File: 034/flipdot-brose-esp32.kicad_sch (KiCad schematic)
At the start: 63 parts, among them J2 Barrel_Jack_Switch, J3 Screw_Terminal_01x02, J5 OLED, J6 TYPE-C-31-M-12, Q11 UMH3N, SW1 CONF, SW2 STAT, SW3 RST, U1 74HCT245, U2 ESP32-WROOM-32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

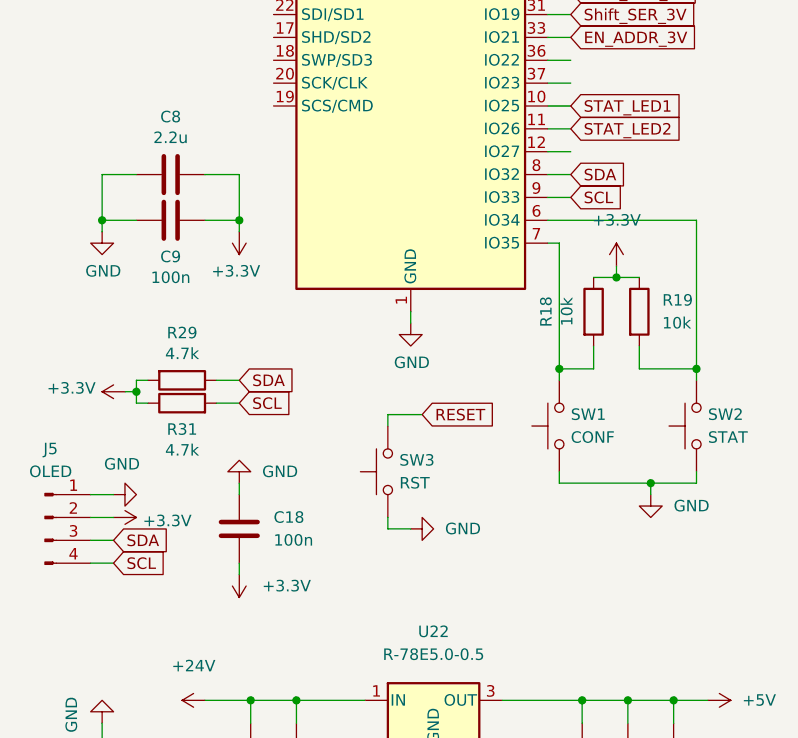
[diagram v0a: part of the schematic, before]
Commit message: fixing naming SDA/SCL
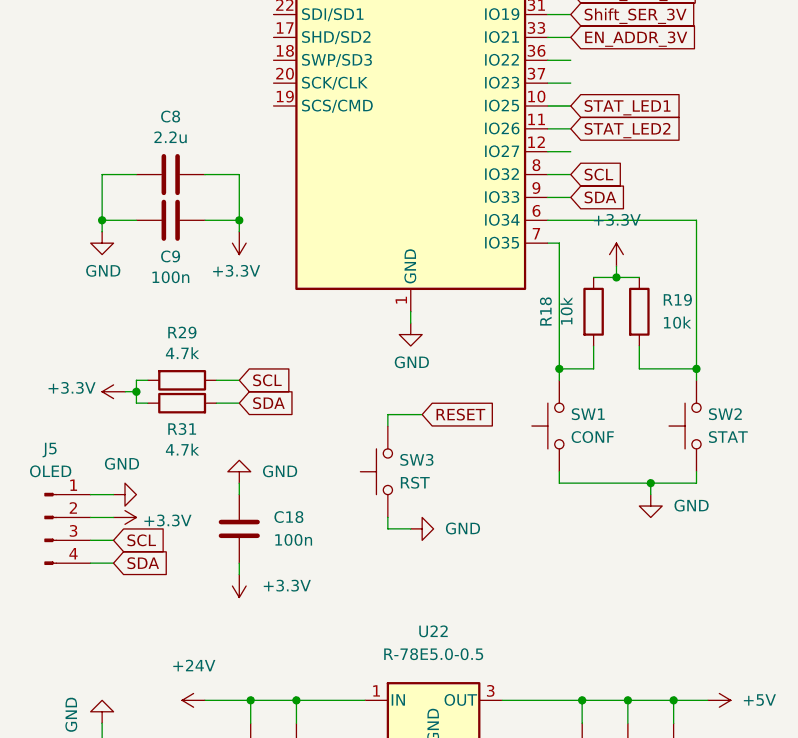
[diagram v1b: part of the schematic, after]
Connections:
- net SCL: now also J5.3 (Pin_3), R29.1, U2.8 (IO32); no longer J5.4 (Pin_4), R31.2, U2.9 (IO33)
- net SDA: now also J5.4 (Pin_4), R31.2, U2.9 (IO33); no longer J5.3 (Pin_3), R29.1, U2.8 (IO32)
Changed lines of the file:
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@@
     (stroke (width 0) (type default) (color 0 0 0 0))
   )
-  (global_label "SDA" (shape input) (at 73.66 80.01 0) (fields_autoplaced)
-    (effects (font (size 1.27 1.27)) (justify left))
-    (property "Intersheet References" "${INTERSHEET_REFS}" (id 0) (at 0 0 0)
-      (effects (font (size 1.27 1.27)) hide)
+  (global_label "SCL" (shape input) (at 73.66 80.01 0) (fields_autoplaced)
+    (effects (font (size 1.27 1.27)) (justify left))
+    (property "Intersheet References" "${INTERSHEET_REFS}" (id 0) (at 79.4918 79.9306 0)
+      (effects (font (size 1.27 1.27)) (justify left) hide)
     )
   )
@@
     )
   )
-  (global_label "SCL" (shape input) (at 36.83 105.41 0) (fields_autoplaced)
-    (effects (font (size 1.27 1.27)) (justify left))
-    (property "Intersheet References" "${INTERSHEET_REFS}" (id 0) (at -12.7 -38.1 0)
-      (effects (font (size 1.27 1.27)) hide)
+  (global_label "SDA" (shape input) (at 36.83 105.41 0) (fields_autoplaced)
+    (effects (font (size 1.27 1.27)) (justify left))
+    (property "Intersheet References" "${INTERSHEET_REFS}" (id 0) (at 42.7223 105.3306 0)
+      (effects (font (size 1.27 1.27)) (justify left) hide)
     )
   )
@@
     )
   )
-  (global_label "SCL" (shape input) (at 22.86 123.19 0) (fields_autoplaced)
-    (effects (font (size 1.27 1.27)) (justify left))
-    (property "Intersheet References" "${INTERSHEET_REFS}" (id 0) (at -26.67 -20.32 0)
-      (effects (font (size 1.27 1.27)) hide)
+  (global_label "SDA" (shape input) (at 22.86 123.19 0) (fields_autoplaced)
+    (effects (font (size 1.27 1.27)) (justify left))
+    (property "Intersheet References" "${INTERSHEET_REFS}" (id 0) (at 28.7523 123.1106 0)
+      (effects (font (size 1.27 1.27)) (justify left) hide)
     )
   )
@@
     )
   )
-  (global_label "SDA" (shape input) (at 22.86 120.65 0) (fields_autoplaced)
-    (effects (font (size 1.27 1.27)) (justify left))
-    (property "Intersheet References" "${INTERSHEET_REFS}" (id 0) (at -26.67 -20.32 0)
-      (effects (font (size 1.27 1.27)) hide)
-    )
-  )
-  (global_label "SDA" (shape input) (at 36.83 102.87 0) (fields_autoplaced)
-    (effects (font (size 1.27 1.27)) (justify left))
-    (property "Intersheet References" "${INTERSHEET_REFS}" (id 0) (at -12.7 -38.1 0)
-      (effects (font (size 1.27 1.27)) hide)
-    )
-  )
-  (global_label "SCL" (shape input) (at 73.66 82.55 0) (fields_autoplaced)
-    (effects (font (size 1.27 1.27)) (justify left))
-    (property "Intersheet References" "${INTERSHEET_REFS}" (id 0) (at 0 0 0)
-      (effects (font (size 1.27 1.27)) hide)
-    )
-  )
+  (global_label "SCL" (shape input) (at 22.86 120.65 0) (fields_autoplaced)
+    (effects (font (size 1.27 1.27)) (justify left))
+    (property "Intersheet References" "${INTERSHEET_REFS}" (id 0) (at 28.6918 120.5706 0)
+      (effects (font (size 1.27 1.27)) (justify left) hide)
+    )
+  )
+  (global_label "SCL" (shape input) (at 36.83 102.87 0) (fields_autoplaced)
+    (effects (font (size 1.27 1.27)) (justify left))
+    (property "Intersheet References" "${INTERSHEET_REFS}" (id 0) (at 42.6618 102.7906 0)
+      (effects (font (size 1.27 1.27)) (justify left) hide)
+    )
+  )
+  (global_label "SDA" (shape input) (at 73.66 82.55 0) (fields_autoplaced)
+    (effects (font (size 1.27 1.27)) (justify left))
+    (property "Intersheet References" "${INTERSHEET_REFS}" (id 0) (at 79.5523 82.4706 0)
+      (effects (font (size 1.27 1.27)) (justify left) hide)
+    )
+  )
